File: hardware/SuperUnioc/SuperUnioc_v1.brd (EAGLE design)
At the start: 92.5 x 80 mm, 71 parts, among them IC1 MAX3232CSE, IC2 ADXRS453BRGZ, IC5 XMEGA128-A1

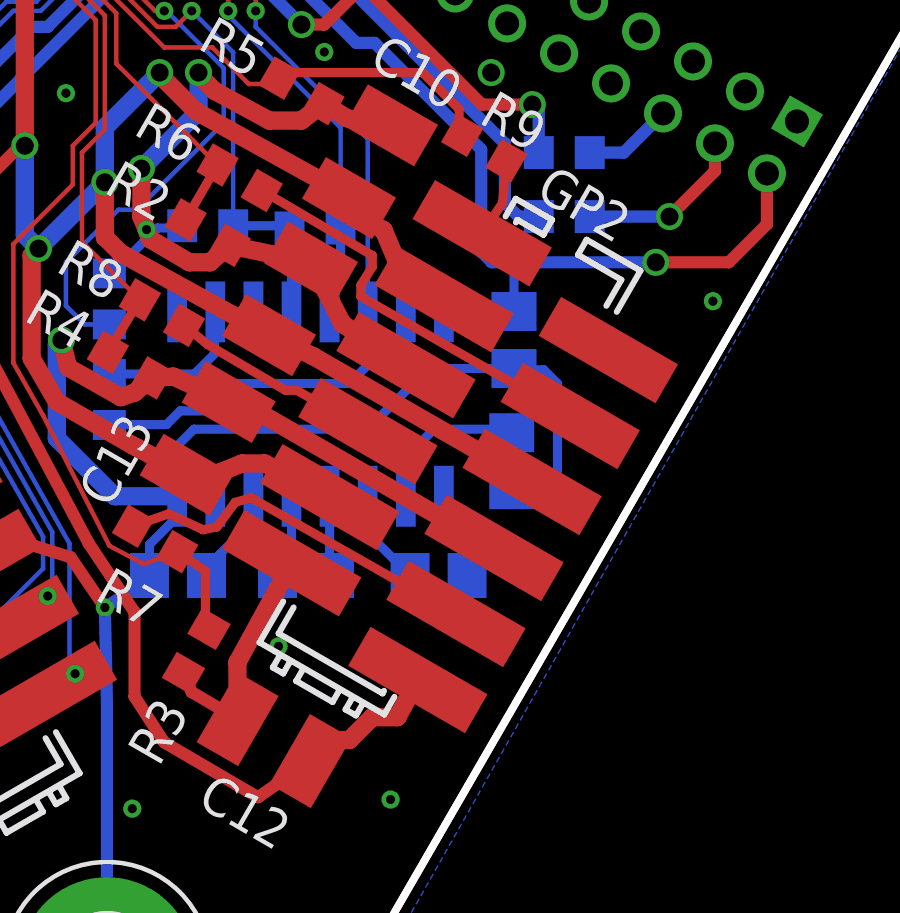
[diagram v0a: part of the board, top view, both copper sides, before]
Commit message: mouser component ref added
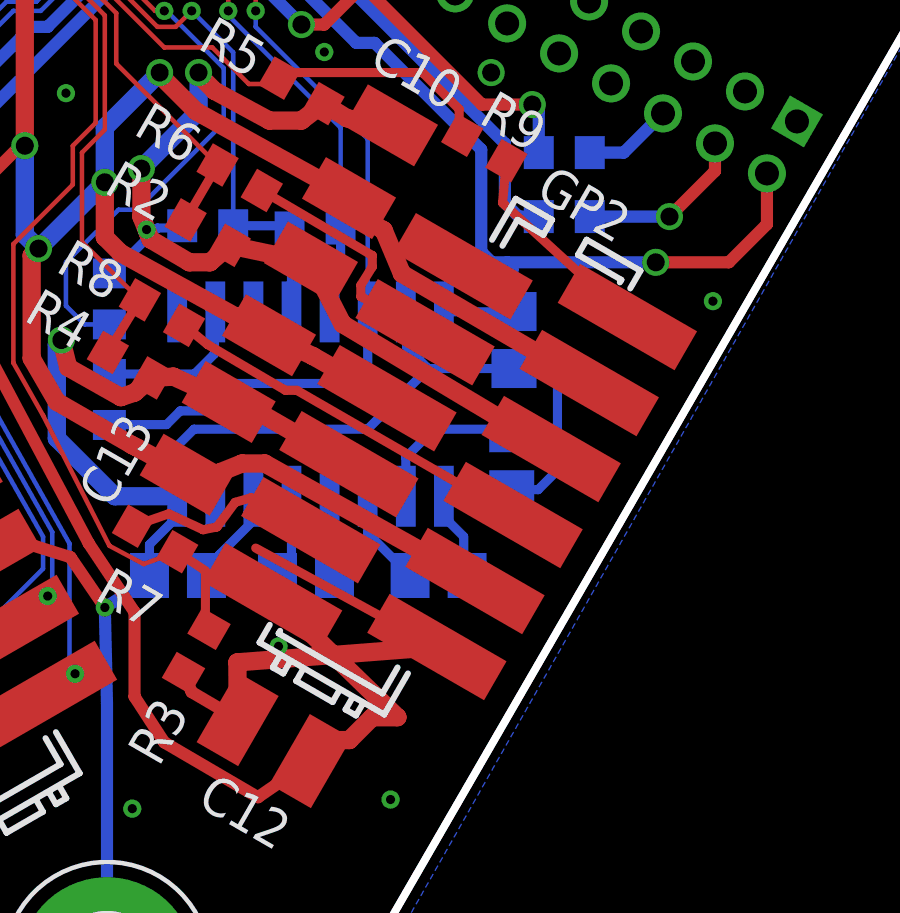
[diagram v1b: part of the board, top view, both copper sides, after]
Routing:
- net +5V: track 270.5 -> 280.4 mm
- net GND: track 455.4 -> 463.8 mm
- net N$24: track 7.14 -> 12.7 mm
- net N$37: track 13.8 -> 8.20 mm
- net N$36: track 12.4 -> 6.83 mm
- net N$22: track 2.63 -> 7.05 mm

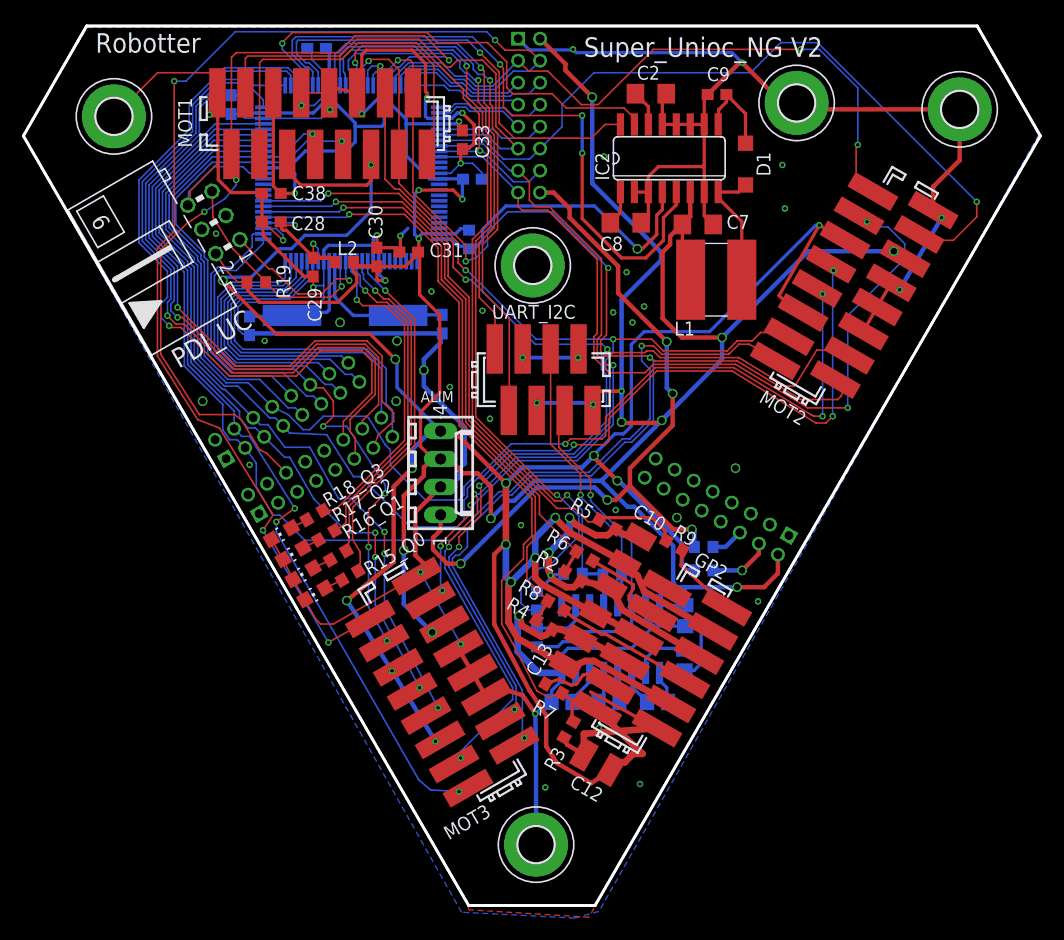
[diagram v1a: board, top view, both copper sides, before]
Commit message: corrected adxrs453 footrpint and gp2 connector footprint
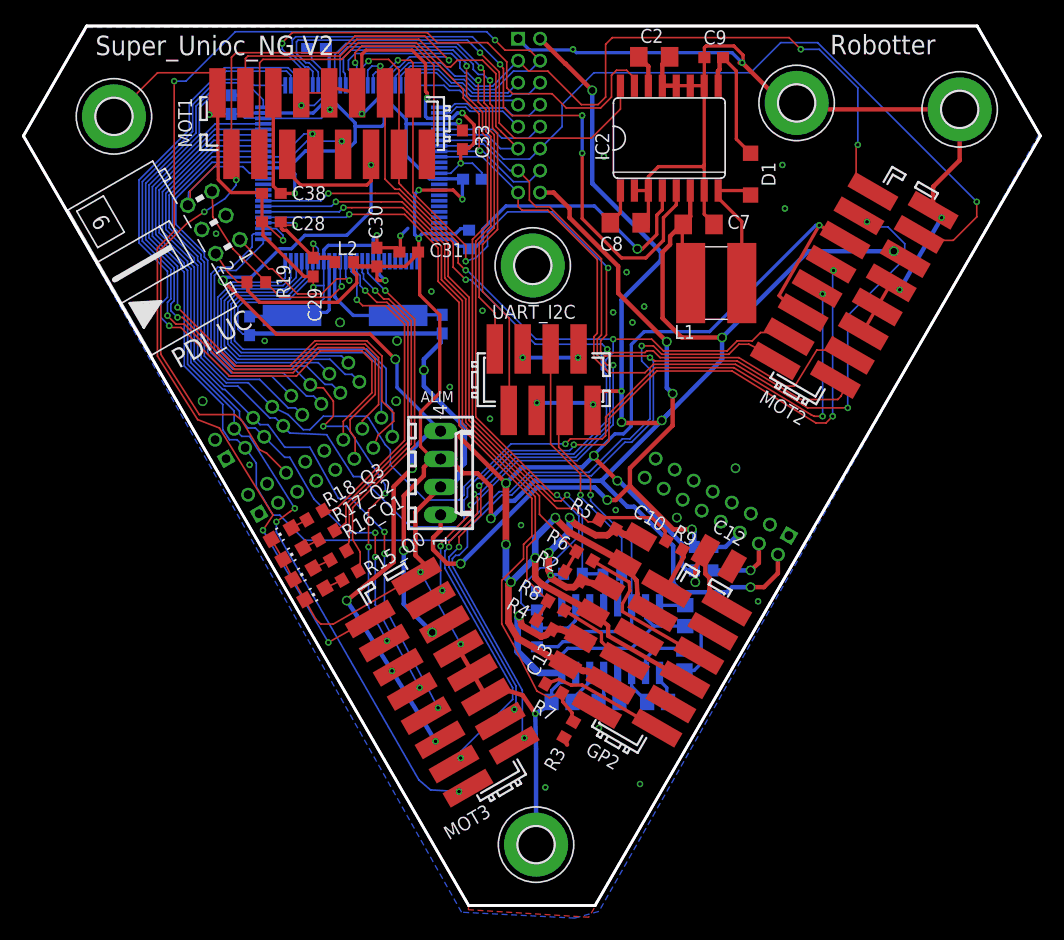
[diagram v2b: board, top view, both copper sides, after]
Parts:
- IC2: device robotter_ic:SO16 -> robotter_ic:SO16_CAV
- R6, R7, R8, R9: value (none) -> 470-F
- moved C12 21.6 mm to (63.2, 31.5), turned to 330 degrees
- moved C2 3.37 mm to (57.4, 77.2)
- moved C9 3.37 mm to (62.8, 77.1)
- moved IC2 1.83 mm to (58.8, 69.8)
- moved D1 1.02 mm to (66.1, 66.5)
- moved L1 0.30 mm to (63.0, 56.6)
- moved C11 0.24 mm to (52.5, 27.8)
- moved C7 0.08 mm to (61.4, 62.0)
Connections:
- net +5V: now also GP2.1, GP2.10, GP2.4, GP2.7; no longer GP2.12, GP2.3, GP2.6, GP2.9
- net GND: now also GP2.12, GP2.3, GP2.6, GP2.9; no longer GP2.11, GP2.2, GP2.5, GP2.8
- net N$22: now also GP2.8, R8.2; no longer GP2.1, R9.2
- net N$24: now also GP2.2, R9.2; no longer GP2.7, R8.2
- net N$36: now also GP2.11; no longer GP2.10
- net N$37: now also GP2.5; no longer GP2.4
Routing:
- net +5V: track 280.4 -> 248.8 mm, vias 15 -> 16
- net GND: track 463.8 -> 439.5 mm
- net N$24: track 12.7 -> 3.91 mm
- net N$37: track 8.20 -> 14.7 mm
- net N$36: track 6.83 -> 11.4 mm
- net N$23: track 8.17 -> 12.5 mm
- net PWM_MOT1_3V3: track 60.7 -> 64.4 mm
- net SCK_ADXRS453_3V3: track 41.4 -> 44.1 mm
- net MOSI_ADXRS453_3V3: track 42.4 -> 45.0 mm
- net N$18: track 11.6 -> 12.4 mm
